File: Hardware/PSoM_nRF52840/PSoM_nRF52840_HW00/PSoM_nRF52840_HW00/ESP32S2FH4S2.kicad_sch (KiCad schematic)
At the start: 31 parts, among them SW401 SW_Push, SW402 SW_Push, U401 ESP32-S2FH4, Y601 Crystal_GND24_Small

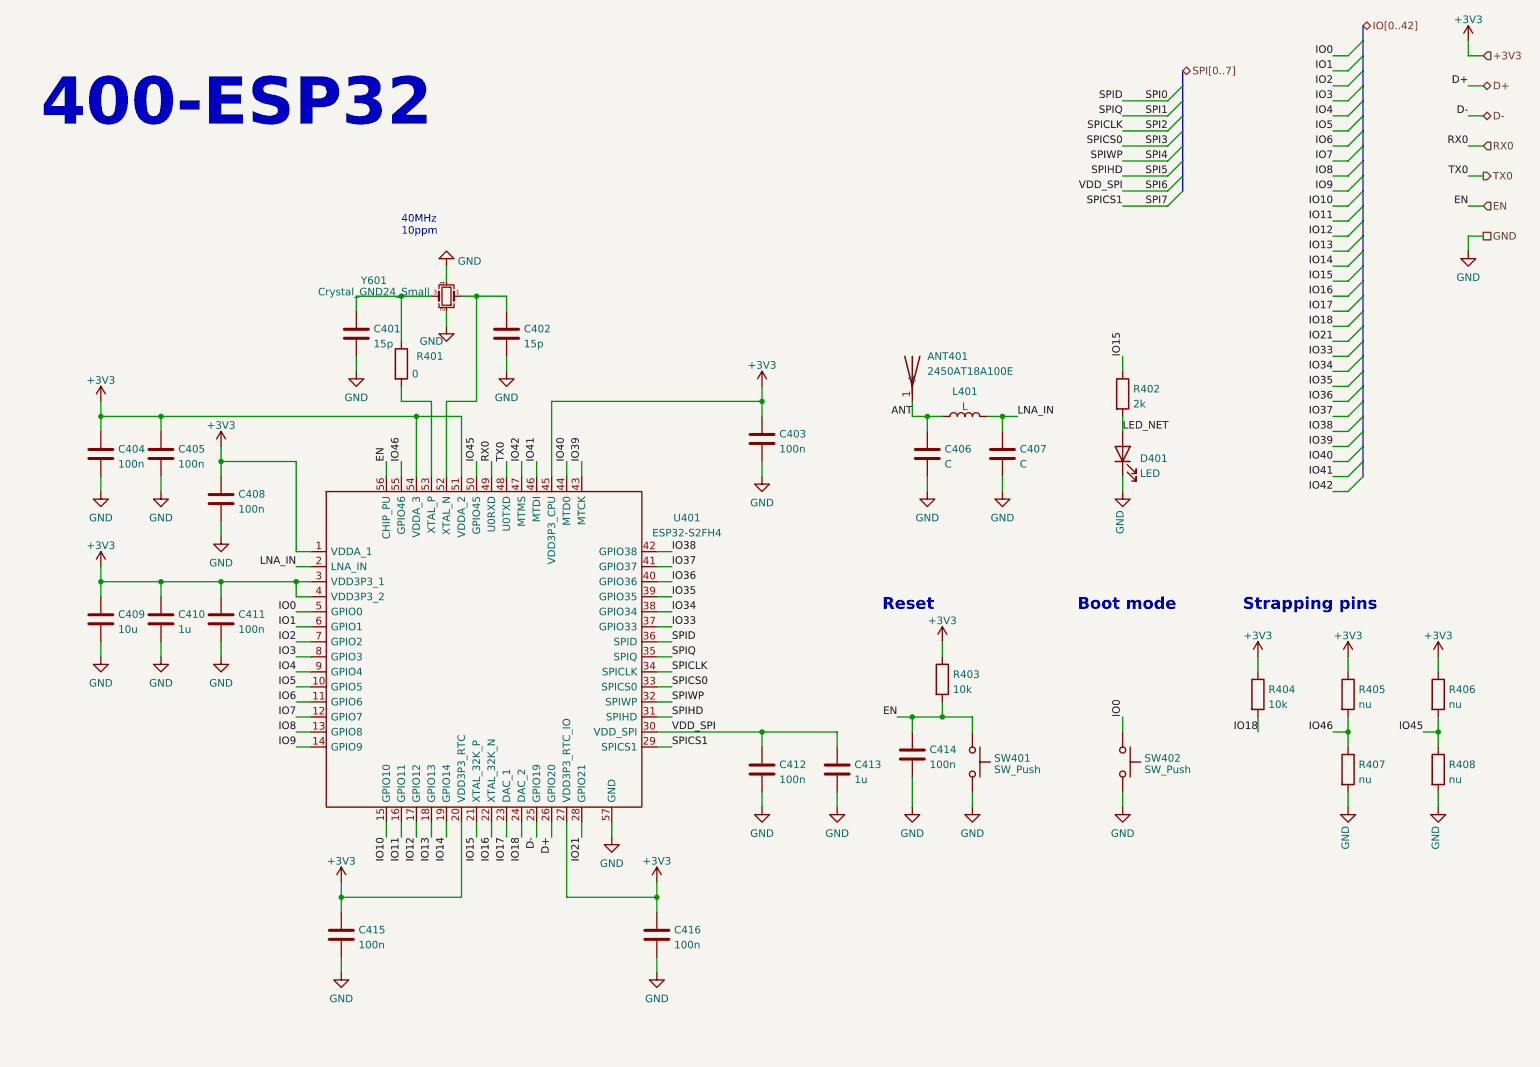
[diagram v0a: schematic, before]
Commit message: started nrf52 schematic
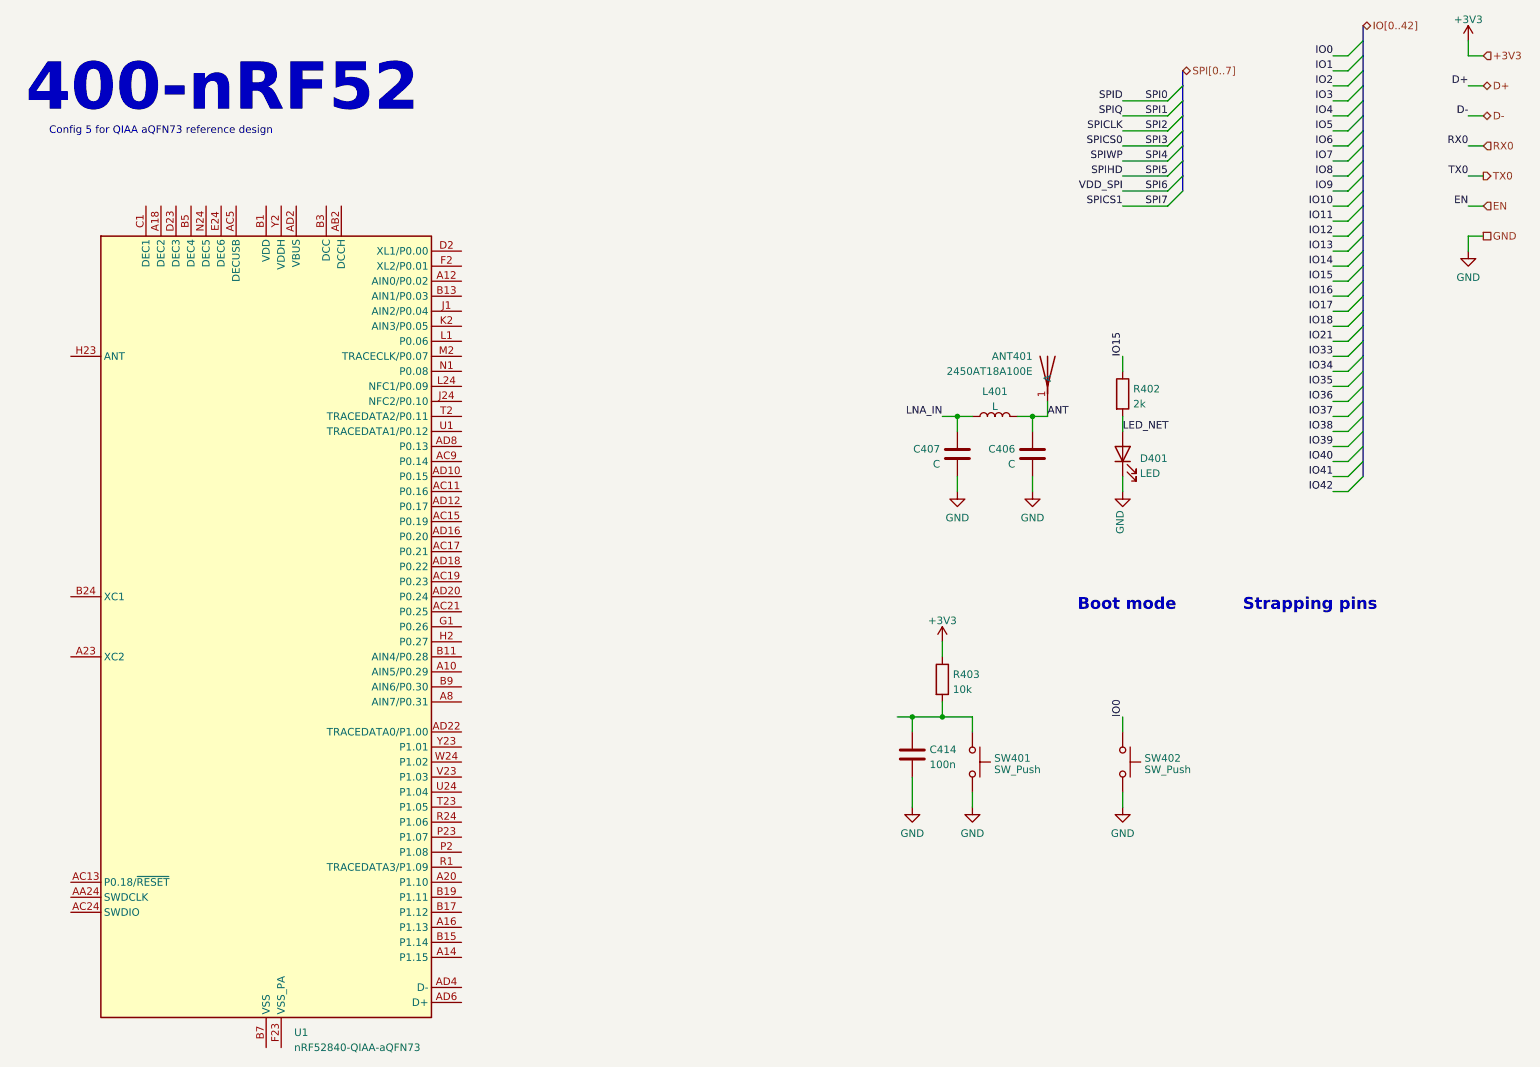
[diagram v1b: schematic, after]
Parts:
- removed C401, C402: 15p, Capacitor_SMD:C_0201_0603Metric, symbol Component lib:C
- removed C403, C404, C405, C408, C411, C412, C415, C416: 100n, Capacitor_SMD:C_0201_0603Metric, symbol Component lib:C
- removed C409: 10u, Capacitor_SMD:C_0603_1608Metric, symbol Component lib:C
- removed C410, C413: 1u, Capacitor_SMD:C_0402_1005Metric, symbol Component lib:C
- removed R401: 0, Resistor_SMD:R_0201_0603Metric, symbol Component lib:R
- removed R404: 10k, Resistor_SMD:R_0201_0603Metric, symbol Component lib:R
- removed R405, R406, R407, R408: nu, Resistor_SMD:R_0201_0603Metric, symbol Component lib:R
- removed U401: ESP32-S2FH4, Component_lib:QFN40P700X700X90-57N-D, symbol Component_lib:ESP32-S2FH4
- removed Y601: Crystal_GND24_Small, Component_lib:Crystal_SMD_2016-4Pin_2.0x1.6mm, symbol Device:Crystal_GND24_Small
- added U1: nRF52840-QIAA-aQFN73, Package_DFN_QFN:Nordic_AQFN-73-1EP_7x7mm_P0.5mm, symbol Component_lib:nRF52840-QIAA-aQFN73
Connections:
- net EN: no longer C414.1, R403.2, SW401.1
- new net: U1.A22 (VDD), U1.AD14 (VDD), U1.AD23 (VDD), U1.B1 (VDD), U1.W1 (VDD)
- new net: U1.B7 (VSS), U1.EP (VSS)
- new net: C414.1, R403.2, SW401.1
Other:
- note added: "400-nRF52"
- note added: "Config 5 for QIAA aQFN73 reference design"
- note removed: "400-ESP32"
- note removed: "40MHz 10ppm"
- note removed: "Reset"
- title: PSoM - ESP32 S2 -> PSoM - nRF52840
- moved on the sheet: ANT401, C406, C407, L401
